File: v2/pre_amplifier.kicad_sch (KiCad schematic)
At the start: 22 parts, among them U19 TLV9151xDBV, U20 TLV9151xDBV

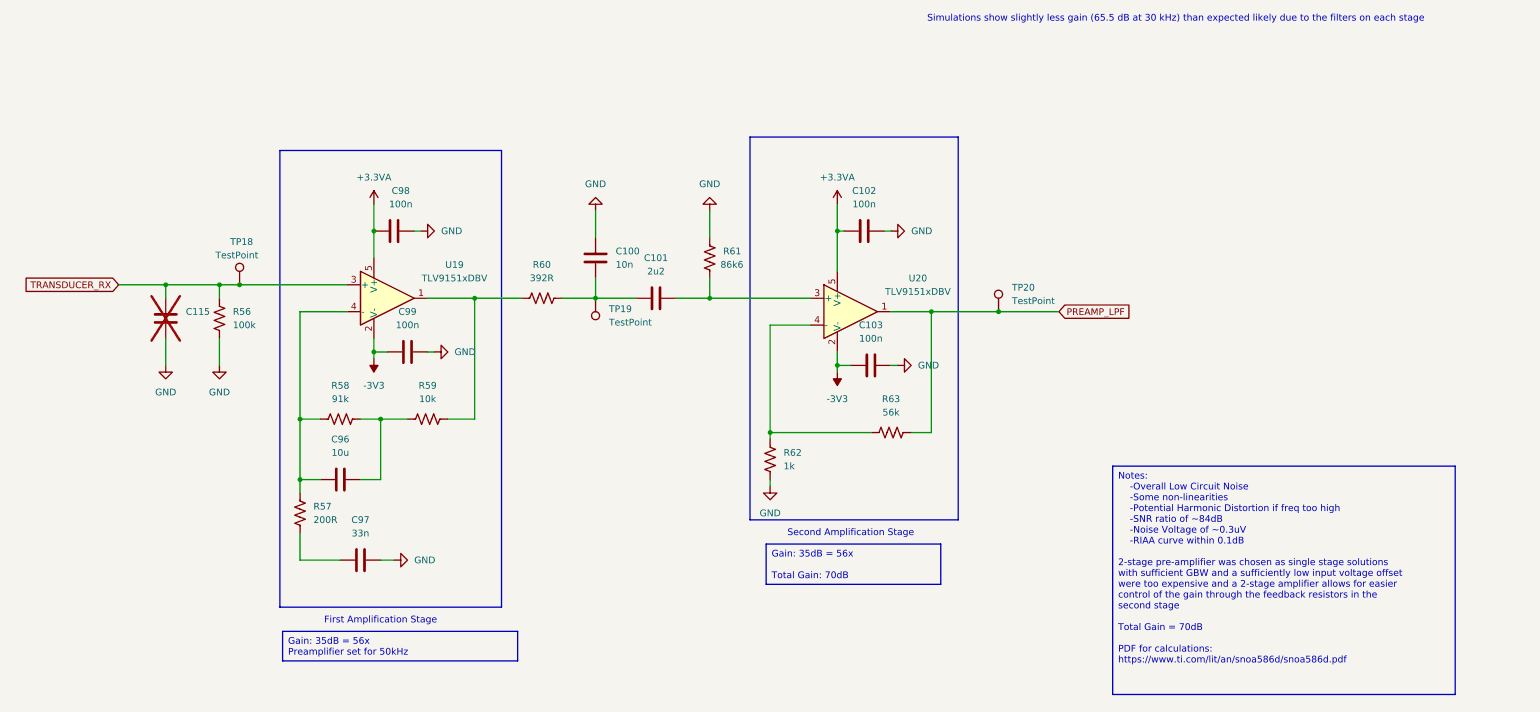
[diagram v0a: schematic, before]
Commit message: Most v2 changes made
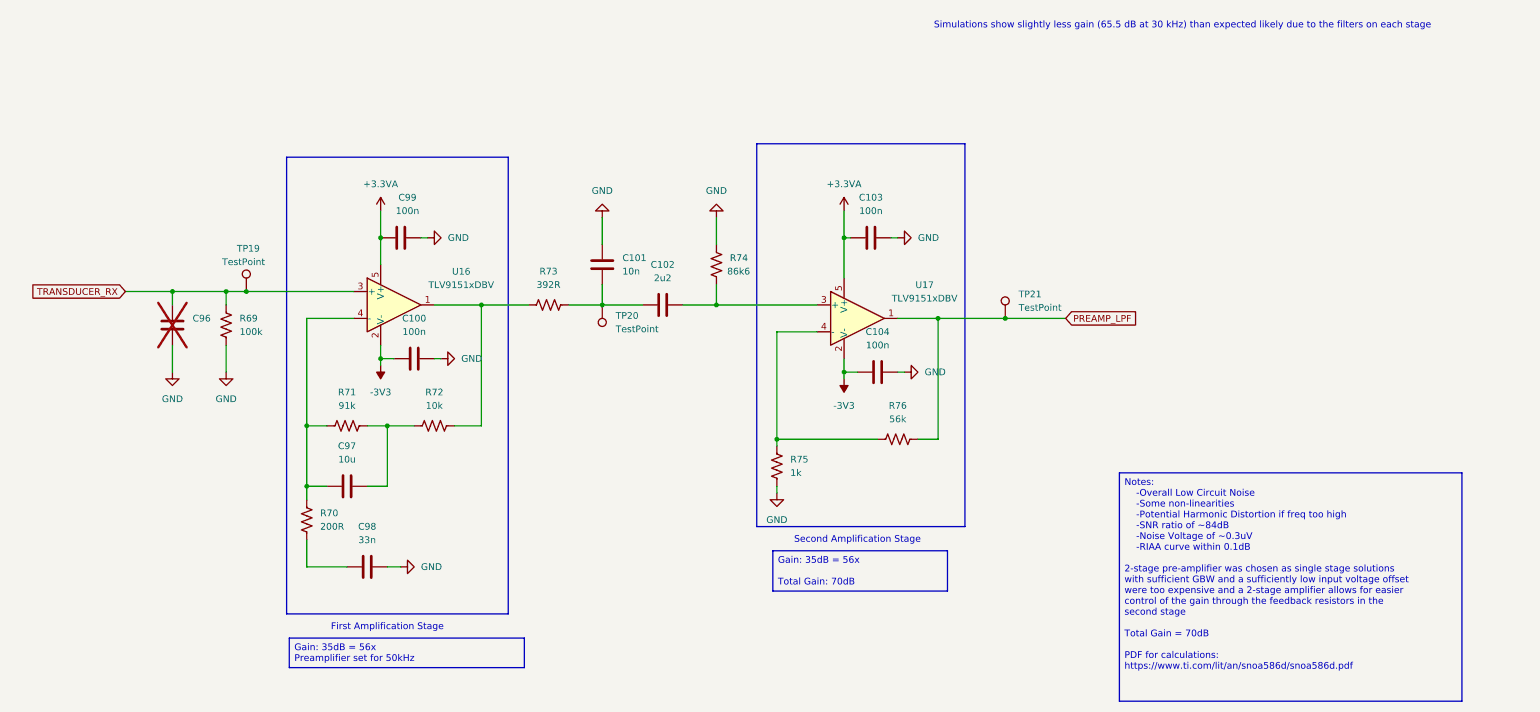
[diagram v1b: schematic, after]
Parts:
- renumbered C99 to C100, C100 to C101, C101 to C102, C102 to C103, C103 to C104, C115 to C96, C96 to C97, C97 to C98, C98 to C99, R56 to R69, R57 to R70, R58 to R71, R59 to R72, R60 to R73, R61 to R74, R62 to R75, R63 to R76, TP18 to TP19, TP19 to TP20, TP20 to TP21, U19 to U16, U20 to U17
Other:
- company: RM -> (none)
- title: Pre-amplifier -> (none)
- moved on the sheet: C100, C101, C102, C103, C104, C96, C97, C98, C99, R69, R70, R71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
